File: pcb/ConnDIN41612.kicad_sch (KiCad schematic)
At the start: 40 parts, among them IC1 SN65HVD75DR, J1 DIN41612_02x32_AC, T1 H1102NL, U3 USBLC6-2SC6, U4 USBLC6-2SC6, U5 USBLC6-2SC6

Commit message: New power design
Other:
- sheet PSU ports: added none; removed REL_Vdrive
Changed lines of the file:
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@@
 	(wire
 		(pts
-			(xy 173.99 63.5) (xy 179.07 63.5)
-		)
-		(stroke
-			(width 0)
-			(type default)
-		)
-	)
-	(wire
-		(pts
 			(xy 212.09 35.56) (xy 212.09 58.42)
 		)
@@
 		)
 	)
-	(hierarchical_label "REL_Vdrive"
-		(shape input)
-		(at 173.99 63.5 180)
-		(effects
-			(font
-				(size 1.27 1.27)
-			)
-			(justify right)
-		)
-	)
 	(symbol
 		(lib_id "Connector:TestPoint")
@@
 	(sheet
 		(at 179.07 45.72)
-		(size 26.67 20.32)
+		(size 26.67 15.24)
 		(exclude_from_sim no)
 		(in_bom yes)
@@
 		)
 		(property "Sheetfile" "PSU.kicad_sch"
-			(at 179.07 66.6246 0)
+			(at 179.07 61.5446 0)
 			(effects
 				(font
@@
 			)
 		)
-		(pin "REL_Vdrive" input
-			(at 179.07 63.5 180)
-			(effects
-				(font
-					(size 1.27 1.27)
-				)
-				(justify left)
-			)
-		)

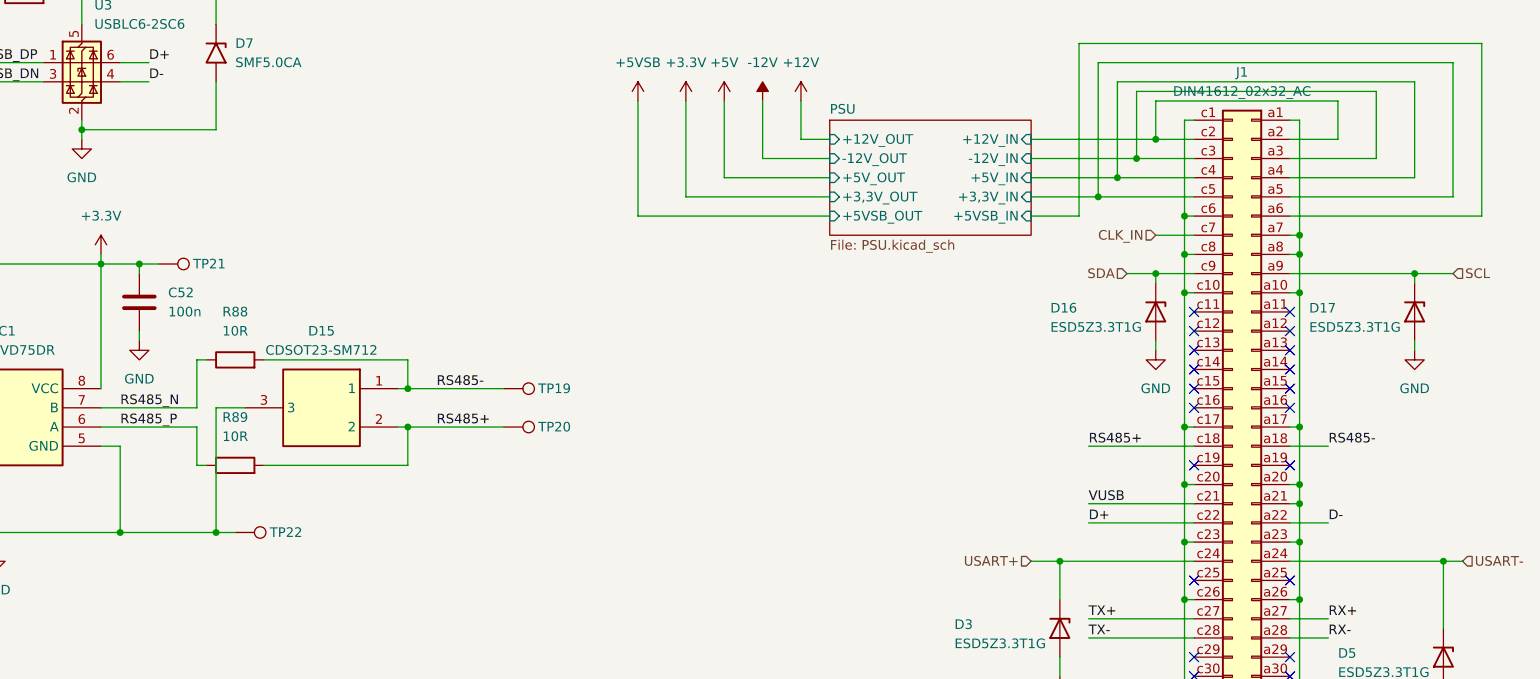
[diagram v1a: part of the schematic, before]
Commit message: Add UniConnector for io expansion (2.0mm pinheader)
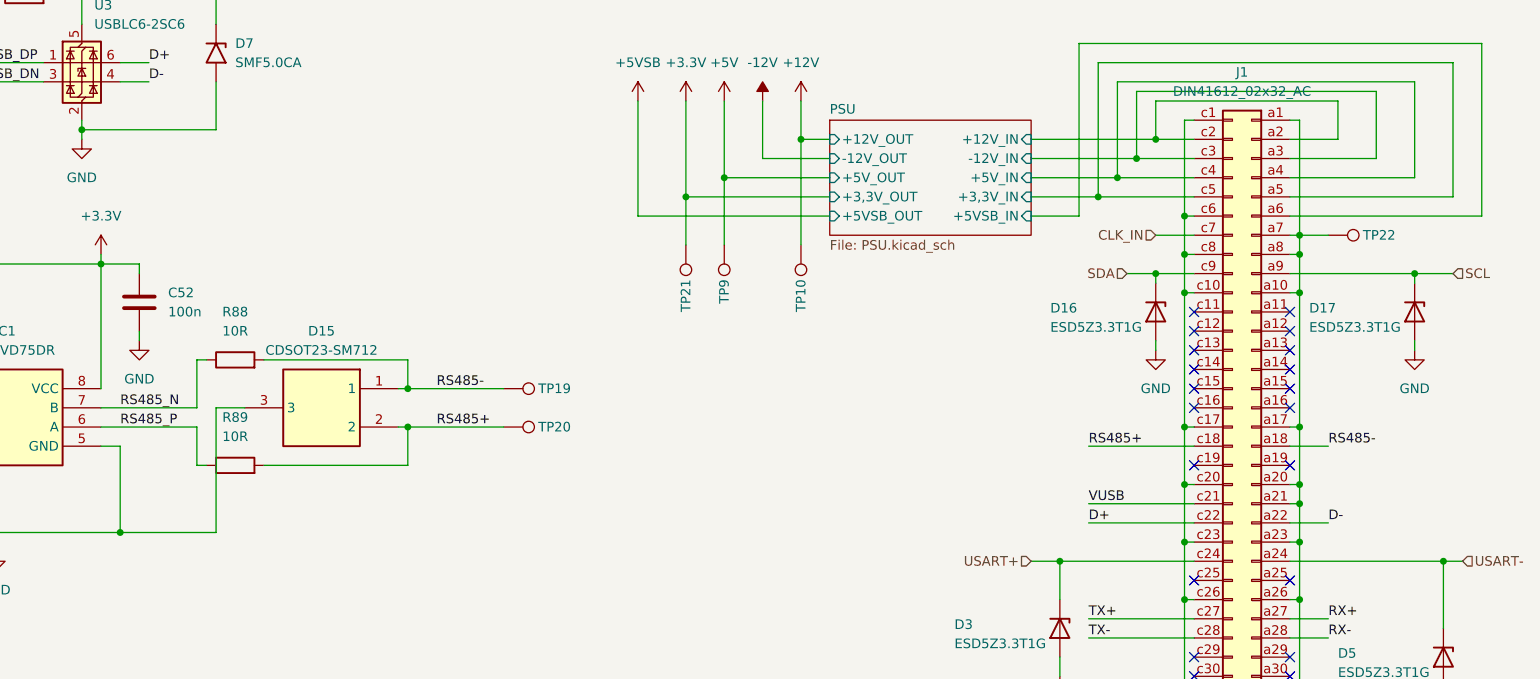
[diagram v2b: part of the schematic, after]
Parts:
- added TP10, TP9: TestPoint, TestPoint:TestPoint_Pad_D1.0mm, symbol Connector:TestPoint
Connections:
- net +12V: now also TP10.1
- net +5V: now also TP9.1
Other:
- moved on the sheet: TP21, TP22
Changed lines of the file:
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@@
 	)
 	(junction
+		(at 165.1 53.34)
+		(diameter 0)
+		(color 0 0 0 0)
+	)
+	(junction
 		(at 260.35 104.14)
 		(diameter 0)
@@
 	)
 	(junction
-		(at 97.79 100.33)
-		(diameter 0)
-		(color 0 0 0 0)
-	)
-	(junction
 		(at 241.3 63.5)
 		(diameter 0)
@@
 	)
 	(junction
-		(at 87.63 64.77)
+		(at 88.9 142.24)
 		(diameter 0)
 		(color 0 0 0 0)
 	)
 	(junction
-		(at 88.9 142.24)
+		(at 43.18 124.46)
 		(diameter 0)
 		(color 0 0 0 0)
 	)
 	(junction
-		(at 43.18 124.46)
+		(at 80.01 29.21)
 		(diameter 0)
 		(color 0 0 0 0)
 	)
 	(junction
-		(at 80.01 29.21)
+		(at 160.02 55.88)
 		(diameter 0)
 		(color 0 0 0 0)
@@
 	)
 	(junction
+		(at 175.26 48.26)
+		(diameter 0)
+		(color 0 0 0 0)
+	)
+	(junction
 		(at 85.09 100.33)
 		(diameter 0)
@@
 	(wire
 		(pts
+			(xy 165.1 53.34) (xy 165.1 62.23)
+		)
+		(stroke
+			(width 0)
+			(type default)
+		)
+	)
+	(wire
+		(pts
 			(xy 160.02 55.88) (xy 179.07 55.88)
 		)
@@
 	(wire
 		(pts
+			(xy 241.3 60.96) (xy 245.11 60.96)
+		)
+		(stroke
+			(width 0)
+			(type default)
+		)
+	)
+	(wire
+		(pts
 			(xy 246.38 124.46) (xy 246.38 128.27)
 		)
@@
 	(wire
 		(pts
-			(xy 97.79 100.33) (xy 100.33 100.33)
-		)
-		(stroke
-			(width 0)
-			(type default)
-		)
-	)
-	(wire
-		(pts
 			(xy 265.43 35.56) (xy 265.43 58.42)
 		)
@@
 	(wire
 		(pts
+			(xy 160.02 55.88) (xy 160.02 62.23)
+		)
+		(stroke
+			(width 0)
+			(type default)
+		)
+	)
+	(wire
+		(pts
+			(xy 175.26 48.26) (xy 175.26 62.23)
+		)
+		(stroke
+			(width 0)
+			(type default)
+		)
+	)
+	(wire
+		(pts
 			(xy 39.37 153.67) (xy 54.61 153.67)
 		)
@@
 	(wire
 		(pts
-			(xy 87.63 64.77) (xy 90.17 64.77)
-		)
-		(stroke
-			(width 0)
-			(type default)
-		)
-	)
-	(wire
-		(pts
 			(xy 50.8 38.1) (xy 58.42 38.1)
 		)
@@
 	(symbol
 		(lib_id "Connector:TestPoint")
-		(at 100.33 100.33 270)
+		(at 245.11 60.96 270)
 		(unit 1)
 		(exclude_from_sim no)
@@
 		(dnp no)
 		(property "Reference" "TP22"
-			(at 104.902 100.33 90)
+			(at 249.682 60.96 90)
 			(effects
 				(font
@@
 		)
 		(property "Value" "TestPoint"
-			(at 105.41 101.5999 90)
+			(at 250.19 62.2299 90)
 			(effects
 				(font
@@
 		)
 		(property "Footprint" "TestPoint:TestPoint_Pad_D1.0mm"
-			(at 100.33 105.41 0)
+			(at 245.11 66.04 0)
 			(effects
 				(font
@@
 		)
 		(property "Datasheet" "~"
-			(at 100.33 105.41 0)
+			(at 245.11 66.04 0)
 			(effects
 				(font
@@
 		)
 		(property "Description" "test point"
-			(at 100.33 100.33 0)
+			(at 245.11 60.96 0)
 			(effects
 				(font
@@
 	)
 	(symbol
+		(lib_id "Connector:TestPoint")
+		(at 175.26 62.23 180)
+		(unit 1)
+		(exclude_from_sim no)
+		(in_bom no)
+		(on_board yes)
+		(dnp no)
+		(property "Reference" "TP10"
+			(at 175.26 66.802 90)
+			(effects
+				(font
+					(size 1.27 1.27)
+				)
+				(justify left)
+			)
+		)
+		(property "Value" "TestPoint"
+			(at 173.9901 67.31 90)
+			(effects
+				(font
+					(size 1.27 1.27)
+				)
+				(justify left)
+				(hide yes)
+			)
+		)
+		(property "Footprint" "TestPoint:TestPoint_Pad_D1.0mm"
+			(at 170.18 62.23 0)
+			(effects
+				(font
+					(size 1.27 1.27)
+				)
+				(hide yes)
+			)
+		)
+		(property "Datasheet" "~"
+			(at 170.18 62.23 0)
+			(effects
+				(font
+					(size 1.27 1.27)
+				)
+				(hide yes)
+			)
+		)
+		(property "Description" "test point"
+			(at 175.26 62.23 0)
+			(effects
+				(font
+					(size 1.27 1.27)
+				)
+				(hide yes)
+			)
+		)
+		(pin "1"
+		)
+		(instances
+			(project "UCB_board"
+				(path "/0c4edb77-9bdf-4103-be66-c5eb9940b163/8ab86091-8037-4e58-8522-0946e4707b6d"
+					(reference "TP10")
+					(unit 1)
+				)
+			)
+		)
+	)
+	(symbol
 		(lib_id "power:GND")
 		(at 50.8 163.83 0)
@@
 	)
 	(symbol
+		(lib_id "Connector:TestPoint")
+		(at 165.1 62.23 180)
+		(unit 1)
+		(exclude_from_sim no)
+		(in_bom no)
+		(on_board yes)
+		(dnp no)
+		(property "Reference" "TP9"
+			(at 165.1 66.802 90)
+			(effects
+				(font
+					(size 1.27 1.27)
+				)
+				(justify left)
+			)
+		)
+		(property "Value" "TestPoint"
+			(at 163.8301 67.31 90)
+			(effects
+				(font
+					(size 1.27 1.27)
+				)
+				(justify left)
+				(hide yes)
+			)
+		)
+		(property "Footprint" "TestPoint:TestPoint_Pad_D1.0mm"
+			(at 160.02 62.23 0)
+			(effects
+				(font
+					(size 1.27 1.27)
+				)
+				(hide yes)
+			)
+		)
+		(property "Datasheet" "~"
+			(at 160.02 62.23 0)
+			(effects
+				(font
+					(size 1.27 1.27)
+				)
+				(hide yes)
+			)
+		)
+		(property "Description" "test point"
+			(at 165.1 62.23 0)
+			(effects
+				(font
+					(size 1.27 1.27)
+				)
+				(hide yes)
+			)
+		)
+		(pin "1"
+		)
+		(instances
+			(project "UCB_board"
+				(path "/0c4edb77-9bdf-4103-be66-c5eb9940b163/8ab86091-8037-4e58-8522-0946e4707b6d"
+					(reference "TP9")
+					(unit 1)
+				)
+			)
+		)
+	)
+	(symbol
 		(lib_id "power:+3.3V")
 		(at 82.55 63.5 0)
@@
 	(symbol
 		(lib_id "Connector:TestPoint")
-		(at 90.17 64.77 270)
+		(at 160.02 62.23 180)
 		(unit 1)
 		(exclude_from_sim no)
@@
 		(dnp no)
 		(property "Reference" "TP21"
-			(at 94.742 64.77 90)
+			(at 160.02 66.802 90)
 			(effects
 				(font
@@
 		)
 		(property "Value" "TestPoint"
-			(at 95.25 66.0399 90)
+			(at 158.7501 67.31 90)
 			(effects
 				(font
@@
 		)
 		(property "Footprint" "TestPoint:TestPoint_Pad_D1.0mm"
-			(at 90.17 69.85 0)
+			(at 154.94 62.23 0)
 			(effects
 				(font
@@
 		)
 		(property "Datasheet" "~"
-			(at 90.17 69.85 0)
+			(at 154.94 62.23 0)
 			(effects
 				(font
@@
 		)
 		(property "Description" "test point"
-			(at 90.17 64.77 0)
+			(at 160.02 62.23 0)
 			(effects
 				(font

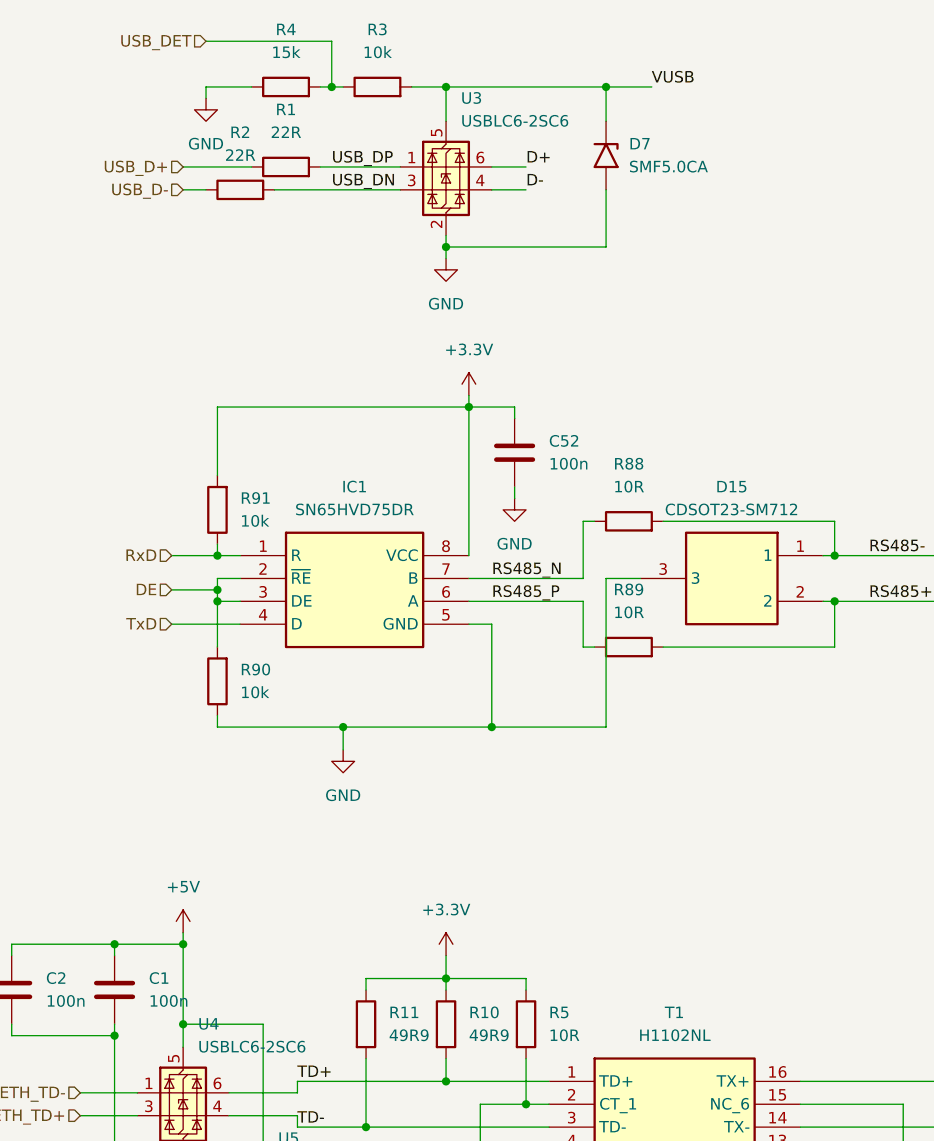
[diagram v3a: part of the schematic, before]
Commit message: Add ferrite beads; update MCU pinout
Schematic and PCB updates: add FerriteBead_Small symbol two instances (FB1, FB2) with matching 0603 inductor footprints on the board. Firmware (.ioc) changes: removed I3C config, added TIM2/TIM5/USART mappings, configured timer channels for input capture, and relabeled pins for the W5500 SPI signals (CS/SCK/MISO/MOSI) plus reset/INT. PCB layout tweaks: new inductor footprint, pad/net reassignments, silkscreen/label coordinate adjustments and various footprint placement/orientation fixes. Also updated board media images and regenerated production files/gerbers.
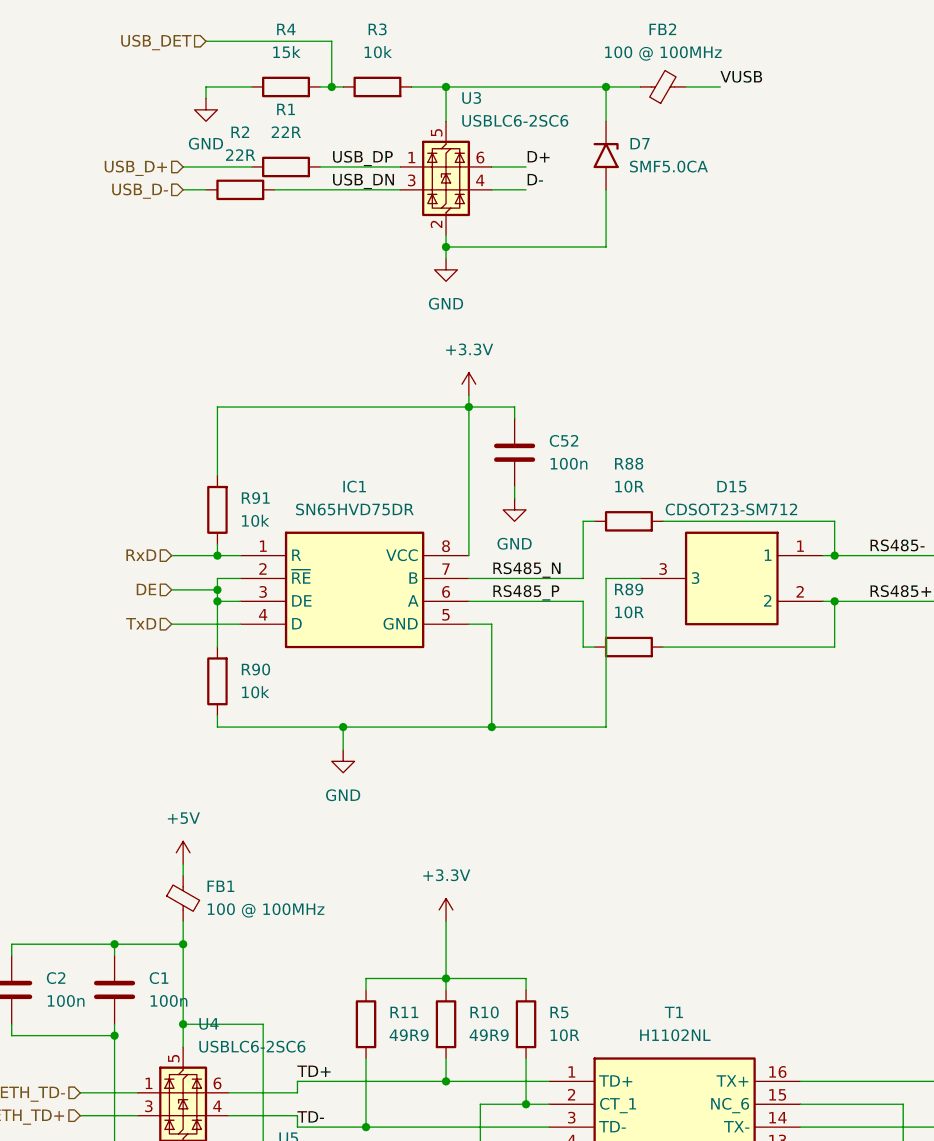
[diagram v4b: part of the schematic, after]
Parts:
- added FB1, FB2: 100 @ 100MHz, Inductor_SMD:L_0603_1608Metric_Pad1.05x0.95mm_HandSolder, symbol Device:FerriteBead_Small
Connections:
- net +5V: now also FB1.1; no longer C1.1, C2.1, U4.5 (VBUS), U5.5 (VBUS)
- net VUSB: now also FB2.2; no longer D7.1 (A1), R3.2, U3.5 (VBUS)
- new net: D7.1 (A1), FB2.1, R3.2, U3.5 (VBUS)
- new net: C1.1, C2.1, FB1.2, U4.5 (VBUS), U5.5 (VBUS)
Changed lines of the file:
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@@
 	(wire
 		(pts
-			(xy 102.87 29.21) (xy 97.79 29.21)
+			(xy 110.49 29.21) (xy 106.68 29.21)
 		)
 		(stroke
@@
 	(wire
 		(pts
+			(xy 50.8 121.92) (xy 50.8 124.46)
+		)
+		(stroke
+			(width 0)
+			(type default)
+		)
+	)
+	(wire
+		(pts
 			(xy 246.38 124.46) (xy 246.38 128.27)
 		)
@@
 	(wire
 		(pts
+			(xy 101.6 29.21) (xy 97.79 29.21)
+		)
+		(stroke
+			(width 0)
+			(type default)
+		)
+	)
+	(wire
+		(pts
 			(xy 138.43 152.4) (xy 138.43 162.56)
 		)
@@
 	(wire
 		(pts
-			(xy 50.8 123.19) (xy 50.8 124.46)
+			(xy 50.8 115.57) (xy 50.8 116.84)
 		)
 		(stroke
@@
 	(wire
 		(pts
-			(xy 80.01 125.73) (xy 80.01 128.27)
+			(xy 80.01 121.92) (xy 80.01 128.27)
 		)
 		(stroke
@@
 	)
 	(label "VUSB"
-		(at 102.87 29.21 0)
+		(at 110.49 29.21 0)
 		(effects
 			(font
@@
 	(symbol
 		(lib_id "power:+3.3V")
-		(at 80.01 125.73 0)
+		(at 80.01 121.92 0)
 		(unit 1)
 		(exclude_from_sim no)
@@
 		(fields_autoplaced yes)
 		(property "Reference" "#PWR024"
-			(at 80.01 129.54 0)
+			(at 80.01 125.73 0)
 			(effects
 				(font
@@
 		)
 		(property "Value" "+3.3V"
-			(at 80.01 120.65 0)
+			(at 80.01 116.84 0)
 			(effects
 				(font
@@
 		)
 		(property "Footprint" ""
-			(at 80.01 125.73 0)
+			(at 80.01 121.92 0)
 			(effects
 				(font
@@
 		)
 		(property "Datasheet" ""
-			(at 80.01 125.73 0)
+			(at 80.01 121.92 0)
 			(effects
 				(font
@@
 		)
 		(property "Description" "Power symbol creates a global label with name \"+3.3V\""
-			(at 80.01 125.73 0)
+			(at 80.01 121.92 0)
 			(effects
 				(font
@@
 	)
 	(symbol
+		(lib_id "Device:FerriteBead_Small")
+		(at 50.8 119.38 0)
+		(unit 1)
+		(exclude_from_sim no)
+		(in_bom yes)
+		(on_board yes)
+		(dnp no)
+		(fields_autoplaced yes)
+		(property "Reference" "FB1"
+			(at 53.34 118.0718 0)
+			(effects
+				(font
+					(size 1.27 1.27)
+				)
+				(justify left)
+			)
+		)
+		(property "Value" "100 @ 100MHz"
+			(at 53.34 120.6118 0)
+			(effects
+				(font
+					(size 1.27 1.27)
+				)
+				(justify left)
+			)
+		)
+		(property "Footprint" "Inductor_SMD:L_0603_1608Metric_Pad1.05x0.95mm_HandSolder"
+			(at 49.022 119.38 90)
+			(effects
+				(font
+					(size 1.27 1.27)
+				)
+				(hide yes)
+			)
+		)
+		(property "Datasheet" "~"
+			(at 50.8 119.38 0)
+			(effects
+				(font
+					(size 1.27 1.27)
+				)
+				(hide yes)
+			)
+		)
+		(property "Description" "WLBD1608HCU101TL"
+			(at 50.8 119.38 0)
+			(effects
+				(font
+					(size 1.27 1.27)
+				)
+				(hide yes)
+			)
+		)
+		(pin "2"
+		)
+		(pin "1"
+		)
+		(instances
+			(project ""
+				(path "/0c4edb77-9bdf-4103-be66-c5eb9940b163/8ab86091-8037-4e58-8522-0946e4707b6d"
+					(reference "FB1")
+					(unit 1)
+				)
+			)
+		)
+	)
+	(symbol
 		(lib_id "Device:C")
 		(at 43.18 129.54 0)
@@
 	)
 	(symbol
+		(lib_id "Device:FerriteBead_Small")
+		(at 104.14 29.21 90)
+		(unit 1)
+		(exclude_from_sim no)
+		(in_bom yes)
+		(on_board yes)
+		(dnp no)
+		(fields_autoplaced yes)
+		(property "Reference" "FB2"
+			(at 104.1019 22.86 90)
+			(effects
+				(font
+					(size 1.27 1.27)
+				)
+			)
+		)
+		(property "Value" "100 @ 100MHz"
+			(at 104.1019 25.4 90)
+			(effects
+				(font
+					(size 1.27 1.27)
+				)
+			)
+		)
+		(property "Footprint" "Inductor_SMD:L_0603_1608Metric_Pad1.05x0.95mm_HandSolder"
+			(at 104.14 30.988 90)
+			(effects
+				(font
+					(size 1.27 1.27)
+				)
+				(hide yes)
+			)
+		)
+		(property "Datasheet" "~"
+			(at 104.14 29.21 0)
+			(effects
+				(font
+					(size 1.27 1.27)
+				)
+				(hide yes)
+			)
+		)
+		(property "Description" "WLBD1608HCU101TL"
+			(at 104.14 29.21 0)
+			(effects
+				(font
+					(size 1.27 1.27)
+				)
+				(hide yes)
+			)
+		)
+		(pin "2"
+		)
+		(pin "1"
+		)
+		(instances
+			(project "UCB_board"
+				(path "/0c4edb77-9bdf-4103-be66-c5eb9940b163/8ab86091-8037-4e58-8522-0946e4707b6d"
+					(reference "FB2")
+					(unit 1)
+				)
+			)
+		)
+	)
+	(symbol
 		(lib_id "power:+12V")
 		(at 175.26 43.18 0)
@@
 	(symbol
 		(lib_id "power:+5V")
-		(at 50.8 123.19 0)
+		(at 50.8 115.57 0)
 		(unit 1)
 		(exclude_from_sim no)
@@
 		(fields_autoplaced yes)
 		(property "Reference" "#PWR017"
-			(at 50.8 127 0)
+			(at 50.8 119.38 0)
 			(effects
 				(font
@@
 		)
 		(property "Value" "+5V"
-			(at 50.8 118.11 0)
+			(at 50.8 110.49 0)
 			(effects
 				(font
@@
 		)
 		(property "Footprint" ""
-			(at 50.8 123.19 0)
+			(at 50.8 115.57 0)
 			(effects
 				(font
@@
 		)
 		(property "Datasheet" ""
-			(at 50.8 123.19 0)
+			(at 50.8 115.57 0)
 			(effects
 				(font
@@
 		)
 		(property "Description" "Power symbol creates a global label with name \"+5V\""
-			(at 50.8 123.19 0)
+			(at 50.8 115.57 0)
 			(effects
 				(font
